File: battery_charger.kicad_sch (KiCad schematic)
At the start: 77 parts, among them J2 Barrel_Jack_Switch_Pin3Ring, Q3 SS8050, Q4 SS8050, U4 TP5100, U5 LM2596S-buck

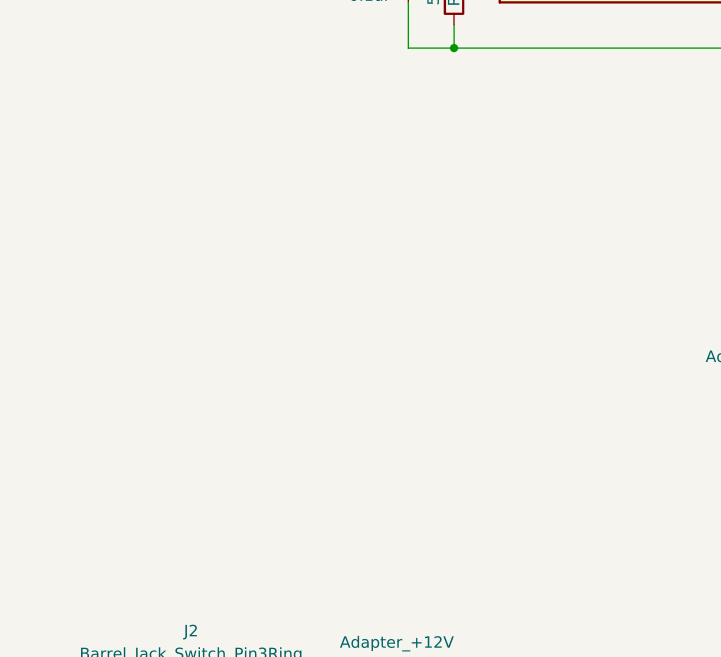
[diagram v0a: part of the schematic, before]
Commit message: Highlighted connectors
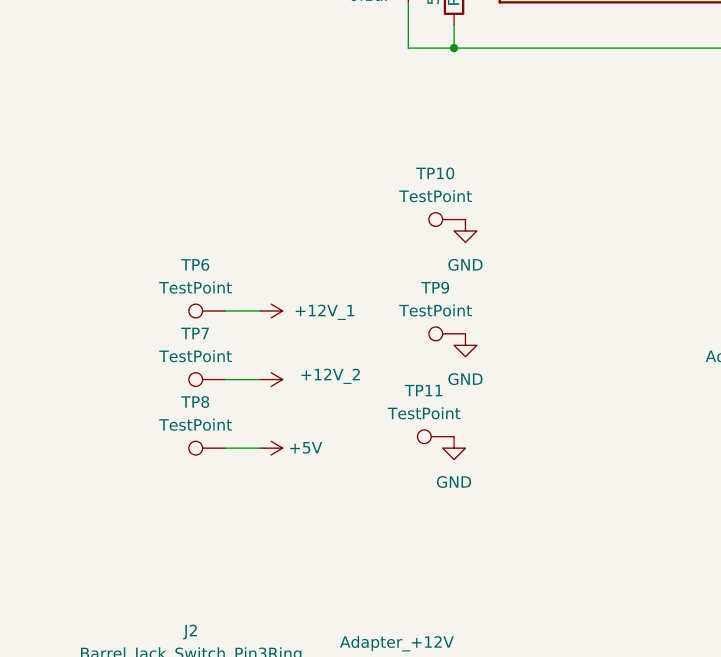
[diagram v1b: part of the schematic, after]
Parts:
- added TP10, TP11, TP6, TP7, TP8, TP9: TestPoint, TestPoint:TestPoint_Pad_D1.0mm, symbol Connector:TestPoint
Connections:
- net +12V_1: now also TP6.1
- net +12V_2: now also TP7.1
- net +5V: now also TP8.1
- net GND: now also TP10.1, TP11.1, TP9.1
